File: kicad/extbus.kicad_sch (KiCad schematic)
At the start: 2 parts, among them J1 BUS Slot #1

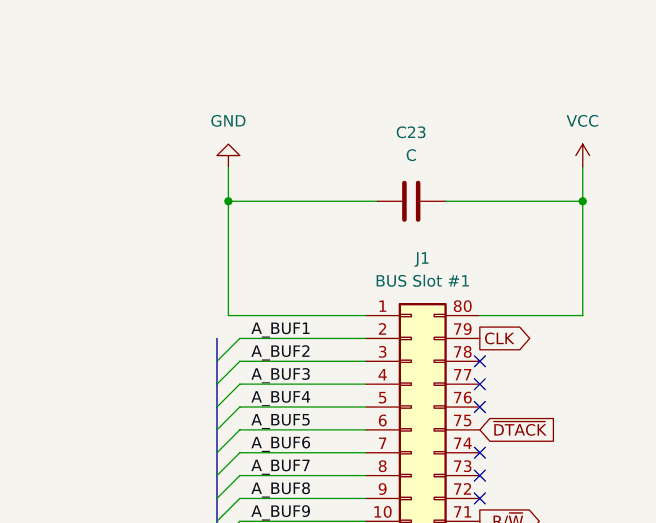
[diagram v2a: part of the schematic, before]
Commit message: added footprints
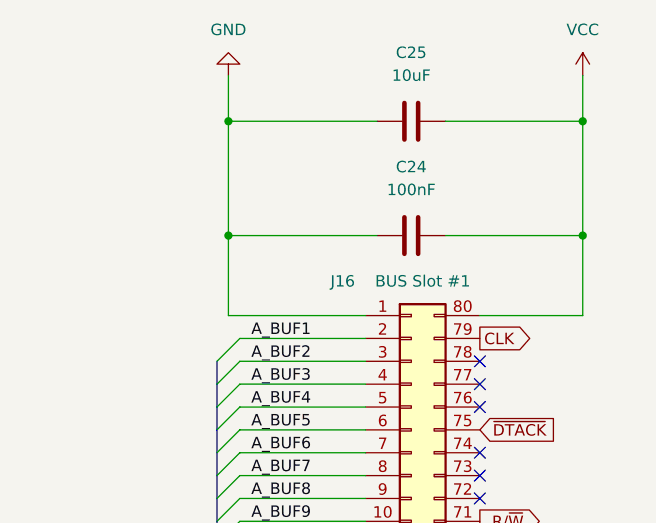
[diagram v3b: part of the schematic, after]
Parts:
- added C25: 10uF, symbol Device:C
- C24: renamed from C23; value C -> 100nF; footprint (none) -> Capacitor_THT:CP_Radial_D5.0mm_P2.50mm
- J16: renamed from J1; footprint (none) -> Connector_PinSocket_2.54mm:PinSocket_2x40_P2.54mm_Vertical
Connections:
- net GND: now also C25.1
- net VCC: now also C25.2
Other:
- moved on the sheet: C24
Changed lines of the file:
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@@
 (kicad_sch (version 20230121) (generator eeschema)
   (paper "A4")
-  (junction (at 54.61 33.02) (diameter 0) (color 0 0 0 0)
-  )
-  (junction (at 93.98 33.02) (diameter 0) (color 0 0 0 0)
+  (junction (at 93.98 24.13) (diameter 0) (color 0 0 0 0)
+  )
+  (junction (at 93.98 36.83) (diameter 0) (color 0 0 0 0)
+  )
+  (junction (at 54.61 36.83) (diameter 0) (color 0 0 0 0)
+  )
+  (junction (at 54.61 24.13) (diameter 0) (color 0 0 0 0)
   )
   (no_connect (at 69.85 137.16))
@@
     (stroke (width 0) (type default))
   )
+  (wire (pts (xy 54.61 24.13) (xy 54.61 36.83))
+    (stroke (width 0) (type default))
+  )
   (bus (pts (xy 93.98 111.76) (xy 93.98 114.3))
     (stroke (width 0) (type default))
   )
-  (wire (pts (xy 54.61 29.21) (xy 54.61 33.02))
-    (stroke (width 0) (type default))
-  )
   (bus (pts (xy 93.98 144.78) (xy 93.98 154.94))
     (stroke (width 0) (type default))
@@
     (stroke (width 0) (type default))
   )
-  (wire (pts (xy 78.74 33.02) (xy 93.98 33.02))
+  (wire (pts (xy 78.74 36.83) (xy 93.98 36.83))
     (stroke (width 0) (type default))
   )
@@
     (stroke (width 0) (type default))
   )
-  (wire (pts (xy 54.61 33.02) (xy 54.61 45.72))
-    (stroke (width 0) (type default))
-  )
   (wire (pts (xy 82.55 104.14) (xy 91.44 104.14))
     (stroke (width 0) (type default))
@@
     (stroke (width 0) (type default))
   )
+  (wire (pts (xy 93.98 24.13) (xy 93.98 36.83))
+    (stroke (width 0) (type default))
+  )
   (bus (pts (xy 53.34 50.8) (xy 53.34 53.34))
     (stroke (width 0) (type default))
@@
     (stroke (width 0) (type default))
   )
-  (wire (pts (xy 93.98 29.21) (xy 93.98 33.02))
-    (stroke (width 0) (type default))
-  )
   (wire (pts (xy 82.55 119.38) (xy 91.44 119.38))
     (stroke (width 0) (type default))
@@
     (stroke (width 0) (type default))
   )
-  (bus (pts (xy 53.34 48.26) (xy 53.34 50.8))
-    (stroke (width 0) (type default))
-  )
   (bus (pts (xy 53.34 104.14) (xy 53.34 106.68))
     (stroke (width 0) (type default))
@@
     (stroke (width 0) (type default))
   )
+  (wire (pts (xy 93.98 36.83) (xy 93.98 45.72))
+    (stroke (width 0) (type default))
+  )
   (bus (pts (xy 53.34 99.06) (xy 53.34 101.6))
     (stroke (width 0) (type default))
@@
     (stroke (width 0) (type default))
   )
+  (wire (pts (xy 54.61 36.83) (xy 54.61 45.72))
+    (stroke (width 0) (type default))
+  )
   (wire (pts (xy 82.55 101.6) (xy 91.44 101.6))
     (stroke (width 0) (type default))
   )
-  (wire (pts (xy 93.98 33.02) (xy 93.98 45.72))
-    (stroke (width 0) (type default))
-  )
   (wire (pts (xy 82.55 106.68) (xy 91.44 106.68))
     (stroke (width 0) (type default))
@@
     (stroke (width 0) (type default))
   )
+  (wire (pts (xy 78.74 24.13) (xy 93.98 24.13))
+    (stroke (width 0) (type default))
+  )
   (wire (pts (xy 55.88 48.26) (xy 69.85 48.26))
     (stroke (width 0) (type default))
@@
     (stroke (width 0) (type default))
   )
+  (wire (pts (xy 93.98 19.05) (xy 93.98 24.13))
+    (stroke (width 0) (type default))
+  )
   (wire (pts (xy 82.55 137.16) (xy 91.44 137.16))
     (stroke (width 0) (type default))
@@
     (stroke (width 0) (type default))
   )
+  (wire (pts (xy 54.61 19.05) (xy 54.61 24.13))
+    (stroke (width 0) (type default))
+  )
   (wire (pts (xy 55.88 66.04) (xy 69.85 66.04))
     (stroke (width 0) (type default))
@@
     (stroke (width 0) (type default))
   )
+  (wire (pts (xy 54.61 24.13) (xy 71.12 24.13))
+    (stroke (width 0) (type default))
+  )
   (wire (pts (xy 55.88 83.82) (xy 69.85 83.82))
     (stroke (width 0) (type default))
@@
     (stroke (width 0) (type default))
   )
-  (wire (pts (xy 71.12 33.02) (xy 54.61 33.02))
+  (wire (pts (xy 71.12 36.83) (xy 54.61 36.83))
     (stroke (width 0) (type default))
   )
@@
     )
   )
-  (symbol (lib_id "power:GND") (at 54.61 29.21 180) (unit 1)
+  (symbol (lib_id "power:GND") (at 54.61 19.05 180) (unit 1)
     (in_bom yes) (on_board yes) (dnp no) (fields_autoplaced)
-    (property "Reference" "#PWR035" (at 54.61 22.86 0)
-      (effects (font (size 1.27 1.27)) hide)
-    )
-    (property "Value" "GND" (at 54.61 24.13 0)
+    (property "Reference" "#PWR063" (at 54.61 12.7 0)
+      (effects (font (size 1.27 1.27)) hide)
+    )
+    (property "Value" "GND" (at 54.61 13.97 0)
       (effects (font (size 1.27 1.27)))
     )
-    (property "Footprint" "" (at 54.61 29.21 0)
-      (effects (font (size 1.27 1.27)) hide)
-    )
-    (property "Datasheet" "" (at 54.61 29.21 0)
+    (property "Footprint" "" (at 54.61 19.05 0)
+      (effects (font (size 1.27 1.27)) hide)
+    )
+    (property "Datasheet" "" (at 54.61 19.05 0)
       (effects (font (size 1.27 1.27)) hide)
     )
@@
       (project "mb68k"
         (path "/e63e39d7-6ac0-4ffd-8aa3-1841a4541b55/6c955f8d-27cd-4aef-8df3-4a7f3323692c"
-          (reference "#PWR035") (unit 1)
+          (reference "#PWR063") (unit 1)
         )
       )
@@
   )
   (symbol (lib_id "Connector_Generic:Conn_02x40_Counter_Clockwise") (at 74.93 93.98 0) (unit 1)
-    (in_bom yes) (on_board yes) (dnp no) (fields_autoplaced)
-    (property "Reference" "J1" (at 76.2 39.37 0)
+    (in_bom yes) (on_board yes) (dnp no)
+    (property "Reference" "J16" (at 67.31 41.91 0)
       (effects (font (size 1.27 1.27)))
     )
@@
       (effects (font (size 1.27 1.27)))
     )
-    (property "Footprint" "" (at 74.93 93.98 0)
+    (property "Footprint" "Connector_PinSocket_2.54mm:PinSocket_2x40_P2.54mm_Vertical" (at 74.93 93.98 0)
       (effects (font (size 1.27 1.27)) hide)
     )
@@
       (project "mb68k"
         (path "/e63e39d7-6ac0-4ffd-8aa3-1841a4541b55/6c955f8d-27cd-4aef-8df3-4a7f3323692c"
-          (reference "J1") (unit 1)
+          (reference "J16") (unit 1)
         )
       )
@@
   (symbol (lib_id "power:VCC") (at 64.77 106.68 90) (unit 1)
     (in_bom yes) (on_board yes) (dnp no) (fields_autoplaced)
-    (property "Reference" "#PWR036" (at 68.58 106.68 0)
+    (property "Reference" "#PWR066" (at 68.58 106.68 0)
       (effects (font (size 1.27 1.27)) hide)
     )
@@
       (project "mb68k"
         (path "/e63e39d7-6ac0-4ffd-8aa3-1841a4541b55/6c955f8d-27cd-4aef-8df3-4a7f3323692c"
-          (reference "#PWR036") (unit 1)
+          (reference "#PWR066") (unit 1)
         )
       )
@@
   (symbol (lib_id "power:GND") (at 91.44 101.6 90) (unit 1)
     (in_bom yes) (on_board yes) (dnp no) (fields_autoplaced)
-    (property "Reference" "#PWR037" (at 97.79 101.6 0)
+    (property "Reference" "#PWR065" (at 97.79 101.6 0)
       (effects (font (size 1.27 1.27)) hide)
     )
@@
       (project "mb68k"
         (path "/e63e39d7-6ac0-4ffd-8aa3-1841a4541b55/6c955f8d-27cd-4aef-8df3-4a7f3323692c"
-          (reference "#PWR037") (unit 1)
+          (reference "#PWR065") (unit 1)
         )
       )
     )
   )
-  (symbol (lib_id "Device:C") (at 74.93 33.02 90) (unit 1)
+  (symbol (lib_id "Device:C") (at 74.93 24.13 90) (unit 1)
     (in_bom yes) (on_board yes) (dnp no) (fields_autoplaced)
-    (property "Reference" "C23" (at 74.93 25.4 90)
+    (property "Reference" "C25" (at 74.93 16.51 90)
       (effects (font (size 1.27 1.27)))
     )
-    (property "Value" "C" (at 74.93 27.94 90)
+    (property "Value" "10uF" (at 74.93 19.05 90)
       (effects (font (size 1.27 1.27)))
     )
-    (property "Footprint" "" (at 78.74 32.0548 0)
-      (effects (font (size 1.27 1.27)) hide)
-    )
-    (property "Datasheet" "~" (at 74.93 33.02 0)
+    (property "Footprint" "" (at 78.74 23.1648 0)
+      (effects (font (size 1.27 1.27)) hide)
+    )
+    (property "Datasheet" "~" (at 74.93 24.13 0)
       (effects (font (size 1.27 1.27)) hide)
     )
@@
       (project "mb68k"
         (path "/e63e39d7-6ac0-4ffd-8aa3-1841a4541b55/6c955f8d-27cd-4aef-8df3-4a7f3323692c"
-          (reference "C23") (unit 1)
+          (reference "C25") (unit 1)
         )
       )
     )
   )
-  (symbol (lib_id "power:VCC") (at 93.98 29.21 0) (unit 1)
+  (symbol (lib_id "Device:C") (at 74.93 36.83 90) (unit 1)
     (in_bom yes) (on_board yes) (dnp no) (fields_autoplaced)
-    (property "Reference" "#PWR034" (at 93.98 33.02 0)
-      (effects (font (size 1.27 1.27)) hide)
-    )
-    (property "Value" "VCC" (at 93.98 24.13 0)
+    (property "Reference" "C24" (at 74.93 29.21 90)
       (effects (font (size 1.27 1.27)))
     )
-    (property "Footprint" "" (at 93.98 29.21 0)
-      (effects (font (size 1.27 1.27)) hide)
-    )
-    (property "Datasheet" "" (at 93.98 29.21 0)
+    (property "Value" "100nF" (at 74.93 31.75 90)
+      (effects (font (size 1.27 1.27)))
+    )
+    (property "Footprint" "Capacitor_THT:CP_Radial_D5.0mm_P2.50mm" (at 78.74 35.8648 0)
+      (effects (font (size 1.27 1.27)) hide)
+    )
+    (property "Datasheet" "~" (at 74.93 36.83 0)
+      (effects (font (size 1.27 1.27)) hide)
+    )
+    (pin "1")
+    (pin "2")
+    (instances
+      (project "mb68k"
+        (path "/e63e39d7-6ac0-4ffd-8aa3-1841a4541b55/6c955f8d-27cd-4aef-8df3-4a7f3323692c"
+          (reference "C24") (unit 1)
+        )
+      )
+    )
+  )
+  (symbol (lib_id "power:VCC") (at 93.98 19.05 0) (unit 1)
+    (in_bom yes) (on_board yes) (dnp no) (fields_autoplaced)
+    (property "Reference" "#PWR064" (at 93.98 22.86 0)
+      (effects (font (size 1.27 1.27)) hide)
+    )
+    (property "Value" "VCC" (at 93.98 13.97 0)
+      (effects (font (size 1.27 1.27)))
+    )
+    (property "Footprint" "" (at 93.98 19.05 0)
+      (effects (font (size 1.27 1.27)) hide)
+    )
+    (property "Datasheet" "" (at 93.98 19.05 0)
       (effects (font (size 1.27 1.27)) hide)
     )
@@
       (project "mb68k"
         (path "/e63e39d7-6ac0-4ffd-8aa3-1841a4541b55/6c955f8d-27cd-4aef-8df3-4a7f3323692c"
-          (reference "#PWR034") (unit 1)
+          (reference "#PWR064") (unit 1)
         )
       )

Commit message: updated readme
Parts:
- added J20, J22: Spare resistors, Connector_PinSocket_2.54mm:PinSocket_1x10_P2.54mm_Vertical, symbol Connector:Conn_01x10_Pin
- added J21: Power bar, Connector_PinSocket_2.54mm:PinSocket_2x11_P2.54mm_Vertical, symbol Connector_Generic:Conn_02x11_Odd_Even
- added R? (x10): 4k7, Resistor_THT:R_Axial_DIN0207_L6.3mm_D2.5mm_P10.16mm_Horizontal, symbol Device:R
- C25: footprint (none) -> Capacitor_THT:CP_Radial_D5.0mm_P2.50mm
- renumbered C24 to C26, J16 to J23
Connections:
- net GND: now also C25.2, C26.2, J23.80 (Pin_80), J21.1 (Pin_1), J21.11 (Pin_11), J21.13 (Pin_13), J21.15 (Pin_15), J21.17 (Pin_17), J21.19 (Pin_19), J21.21 (Pin_21), J21.3 (Pin_3), J21.5 (Pin_5), J21.7 (Pin_7), J21.9 (Pin_9); no longer C25.1, C26.1, J23.1 (Pin_1)
- net VCC: now also C25.1, C26.1, J23.1 (Pin_1), J21.10 (Pin_10), J21.12 (Pin_12), J21.14 (Pin_14), J21.16 (Pin_16), J21.18 (Pin_18), J21.2 (Pin_2), J21.20 (Pin_20), J21.22 (Pin_22), J21.4 (Pin_4), J21.6 (Pin_6), J21.8 (Pin_8); no longer C25.2, C26.2, J23.80 (Pin_80)
- new net: J20.1 (Pin_1), R?.2
- new net: J20.10 (Pin_10), R?.2
- new net: J20.2 (Pin_2), R?.2
- new net: J20.3 (Pin_3), R?.2
- new net: J20.4 (Pin_4), R?.2
- new net: J20.5 (Pin_5), R?.2
- new net: J20.6 (Pin_6), R?.2
- new net: J20.7 (Pin_7), R?.2
- new net: J20.8 (Pin_8), R?.2
- new net: J20.9 (Pin_9), R?.2
- new net: J22.1 (Pin_1), R?.1
- new net: J22.10 (Pin_10), R?.1
- new net: J22.2 (Pin_2), R?.1
- new net: J22.3 (Pin_3), R?.1
- new net: J22.4 (Pin_4), R?.1
- new net: J22.5 (Pin_5), R?.1
- new net: J22.6 (Pin_6), R?.1
- new net: J22.7 (Pin_7), R?.1
- new net: J22.8 (Pin_8), R?.1
- new net: J22.9 (Pin_9), R?.1
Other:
- note added: "Extra pullup / pulldowns for debug/experiment"
- title: (none) -> Mats Brorson 68010 SBC External Bus
- moved on the sheet: C25, C26, J23

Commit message: PCB to ATX size
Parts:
- removed J23: BUS Slot #1, Connector_PinSocket_2.54mm:PinSocket_2x40_P2.54mm_Vertical, symbol Connector_Generic:Conn_02x40_Counter_Clockwise
- added C14: 10uF, Capacitor_THT:CP_Radial_D5.0mm_P2.50mm, symbol Device:C
- added C15: 100nF, Capacitor_THT:CP_Radial_D5.0mm_P2.50mm, symbol Device:C
- added J23: BUS Slot 2, Connector_PinSocket_2.54mm:PinSocket_2x40_P2.54mm_Vertical, symbol Connector_Generic:Conn_02x40_Odd_Even
- added J24: BUS Slot 1, Connector_PinSocket_2.54mm:PinSocket_2x40_P2.54mm_Vertical, symbol Connector_Generic:Conn_02x40_Odd_Even
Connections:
- net CLK: now also J23.4 (Pin_4), J24.4 (Pin_4)
- net GND: now also J21.10 (Pin_10), J21.12 (Pin_12), J21.14 (Pin_14), J21.16 (Pin_16), J21.18 (Pin_18), J21.2 (Pin_2), J21.20 (Pin_20), J21.22 (Pin_22), J21.4 (Pin_4), J21.6 (Pin_6), J21.8 (Pin_8), C14.2, C15.2, J23.2 (Pin_2), J23.46 (Pin_46), J24.2 (Pin_2), J24.46 (Pin_46); no longer J21.1 (Pin_1), J21.11 (Pin_11), J21.13 (Pin_13), J21.15 (Pin_15), J21.17 (Pin_17), J21.19 (Pin_19), J21.21 (Pin_21), J21.3 (Pin_3), J21.5 (Pin_5), J21.7 (Pin_7), J21.9 (Pin_9)
- net VCC: now also J21.1 (Pin_1), J21.11 (Pin_11), J21.13 (Pin_13), J21.15 (Pin_15), J21.17 (Pin_17), J21.19 (Pin_19), J21.21 (Pin_21), J21.3 (Pin_3), J21.5 (Pin_5), J21.7 (Pin_7), J21.9 (Pin_9), C14.1, C15.1, J23.1 (Pin_1), J23.49 (Pin_49), J24.1 (Pin_1), J24.49 (Pin_49); no longer J21.10 (Pin_10), J21.12 (Pin_12), J21.14 (Pin_14), J21.16 (Pin_16), J21.18 (Pin_18), J21.2 (Pin_2), J21.20 (Pin_20), J21.22 (Pin_22), J21.4 (Pin_4), J21.6 (Pin_6), J21.8 (Pin_8)
- net _R/~{W}: now also J23.20 (Pin_20), J24.20 (Pin_20)
- net ~{DTACK}: now also J23.12 (Pin_12), J24.12 (Pin_12)
- net ~{IACK1}: now also J23.51 (Pin_51), J24.51 (Pin_51)
- net ~{IACK2}: now also J23.53 (Pin_53), J24.53 (Pin_53)
- net ~{IACK3}: now also J23.55 (Pin_55), J24.55 (Pin_55)
- net ~{IACK4}: now also J23.57 (Pin_57), J24.57 (Pin_57)
- net ~{IACK5}: now also J23.59 (Pin_59), J24.59 (Pin_59)
- net ~{IACK6}: now also J23.61 (Pin_61), J24.61 (Pin_61)
- net ~{IACK7}: now also J23.63 (Pin_63), J24.63 (Pin_63)
- net ~{IRQ1}: now also J23.32 (Pin_32), J24.32 (Pin_32)
- net ~{IRQ2}: now also J23.34 (Pin_34), J24.34 (Pin_34)
- net ~{IRQ3}: now also J23.36 (Pin_36), J24.36 (Pin_36)
- net ~{IRQ4}: now also J23.38 (Pin_38), J24.38 (Pin_38)
- net ~{IRQ5}: now also J23.40 (Pin_40), J24.40 (Pin_40)
- net ~{IRQ6}: now also J23.42 (Pin_42), J24.42 (Pin_42)
- net ~{IRQ7}: now also J23.44 (Pin_44), J24.44 (Pin_44)
- net ~{_AS}: now also J23.26 (Pin_26), J24.26 (Pin_26)
- net ~{_LDS}: now also J23.22 (Pin_22), J24.22 (Pin_22)
- net ~{_UDS}: now also J23.24 (Pin_24), J24.24 (Pin_24)
- new net A1: J23.47 (Pin_47), J24.47 (Pin_47)
- new net A10: J23.29 (Pin_29), J24.29 (Pin_29)
- new net A11: J23.27 (Pin_27), J24.27 (Pin_27)
- new net A12: J23.25 (Pin_25), J24.25 (Pin_25)
- new net A13: J23.23 (Pin_23), J24.23 (Pin_23)
- new net A14: J23.21 (Pin_21), J24.21 (Pin_21)
- new net A15: J23.19 (Pin_19), J24.19 (Pin_19)
- new net A16: J23.17 (Pin_17), J24.17 (Pin_17)
- new net A17: J23.15 (Pin_15), J24.15 (Pin_15)
- new net A18: J23.13 (Pin_13), J24.13 (Pin_13)
- new net A19: J23.11 (Pin_11), J24.11 (Pin_11)
- new net A2: J23.45 (Pin_45), J24.45 (Pin_45)
- new net A20: J23.9 (Pin_9), J24.9 (Pin_9)
- new net A21: J23.7 (Pin_7), J24.7 (Pin_7)
- new net A22: J23.5 (Pin_5), J24.5 (Pin_5)
- new net A23: J23.3 (Pin_3), J24.3 (Pin_3)
- new net A3: J23.43 (Pin_43), J24.43 (Pin_43)
- new net A4: J23.41 (Pin_41), J24.41 (Pin_41)
- new net A5: J23.39 (Pin_39), J24.39 (Pin_39)
- new net A6: J23.37 (Pin_37), J24.37 (Pin_37)
- new net A7: J23.35 (Pin_35), J24.35 (Pin_35)
- new net A8: J23.33 (Pin_33), J24.33 (Pin_33)
- new net A9: J23.31 (Pin_31), J24.31 (Pin_31)
- new net D0: J23.78 (Pin_78), J24.78 (Pin_78)
- new net D1: J23.76 (Pin_76), J24.76 (Pin_76)
- new net D10: J23.58 (Pin_58), J24.58 (Pin_58)
- new net D11: J23.56 (Pin_56), J24.56 (Pin_56)
- new net D12: J23.54 (Pin_54), J24.54 (Pin_54)
- new net D13: J23.52 (Pin_52), J24.52 (Pin_52)
- new net D14: J23.50 (Pin_50), J24.50 (Pin_50)
- new net D15: J23.48 (Pin_48), J24.48 (Pin_48)
- new net D2: J23.74 (Pin_74), J24.74 (Pin_74)
- new net D3: J23.72 (Pin_72), J24.72 (Pin_72)
- new net D4: J23.70 (Pin_70), J24.70 (Pin_70)
- new net D5: J23.68 (Pin_68), J24.68 (Pin_68)
- new net D6: J23.66 (Pin_66), J24.66 (Pin_66)
- new net D7: J23.64 (Pin_64), J24.64 (Pin_64)
- new net D8: J23.62 (Pin_62), J24.62 (Pin_62)
- new net D9: J23.60 (Pin_60), J24.60 (Pin_60)
- no-connect marks 17 -> 34

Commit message: saving state
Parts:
- removed J21: Power bar, Connector_PinSocket_2.54mm:PinSocket_2x11_P2.54mm_Vertical, symbol Connector_Generic:Conn_02x11_Odd_Even
- added J21: Power bar, Connector_PinSocket_2.54mm:PinSocket_2x10_P2.54mm_Vertical, symbol Connector_Generic:Conn_02x10_Odd_Even
- C25: footprint Capacitor_THT:CP_Radial_D5.0mm_P2.50mm -> Capacitor_THT:C_Disc_D5.0mm_W2.5mm_P2.50mm
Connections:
- net D0: now also J23.40 (Pin_40), J24.40 (Pin_40); no longer J23.78 (Pin_78), J24.78 (Pin_78)
- net D1: now also J23.38 (Pin_38), J24.38 (Pin_38); no longer J23.76 (Pin_76), J24.76 (Pin_76)
- net D10: now also J23.68 (Pin_68), J24.68 (Pin_68); no longer J23.58 (Pin_58), J24.58 (Pin_58)
- net D11: now also J23.70 (Pin_70), J24.70 (Pin_70); no longer J23.56 (Pin_56), J24.56 (Pin_56)
- net D12: now also J23.72 (Pin_72), J24.72 (Pin_72); no longer J23.54 (Pin_54), J24.54 (Pin_54)
- net D13: now also J23.74 (Pin_74), J24.74 (Pin_74); no longer J23.52 (Pin_52), J24.52 (Pin_52)
- net D14: now also J23.76 (Pin_76), J24.76 (Pin_76); no longer J23.50 (Pin_50), J24.50 (Pin_50)
- net D15: now also J23.78 (Pin_78), J24.78 (Pin_78); no longer J23.48 (Pin_48), J24.48 (Pin_48)
- net D2: now also J23.36 (Pin_36), J24.36 (Pin_36); no longer J23.74 (Pin_74), J24.74 (Pin_74)
- net D3: now also J23.34 (Pin_34), J24.34 (Pin_34); no longer J23.72 (Pin_72), J24.72 (Pin_72)
- net D4: now also J23.32 (Pin_32), J24.32 (Pin_32); no longer J23.70 (Pin_70), J24.70 (Pin_70)
- net D5: now also J23.58 (Pin_58), J24.58 (Pin_58); no longer J23.68 (Pin_68), J24.68 (Pin_68)
- net D6: now also J23.60 (Pin_60), J24.60 (Pin_60); no longer J23.66 (Pin_66), J24.66 (Pin_66)
- net D7: now also J23.62 (Pin_62), J24.62 (Pin_62); no longer J23.64 (Pin_64), J24.64 (Pin_64)
- net D8: now also J23.64 (Pin_64), J24.64 (Pin_64); no longer J23.62 (Pin_62), J24.62 (Pin_62)
- net D9: now also J23.66 (Pin_66), J24.66 (Pin_66); no longer J23.60 (Pin_60), J24.60 (Pin_60)
- net GND: now also J23.42 (Pin_42), J24.42 (Pin_42), J21.10 (Pin_10), J21.12 (Pin_12), J21.14 (Pin_14), J21.16 (Pin_16), J21.18 (Pin_18), J21.2 (Pin_2), J21.20 (Pin_20), J21.4 (Pin_4), J21.6 (Pin_6), J21.8 (Pin_8); no longer J23.46 (Pin_46), J24.46 (Pin_46)
- net VCC: now also J21.1 (Pin_1), J21.11 (Pin_11), J21.13 (Pin_13), J21.15 (Pin_15), J21.17 (Pin_17), J21.19 (Pin_19), J21.3 (Pin_3), J21.5 (Pin_5), J21.7 (Pin_7), J21.9 (Pin_9)
- net ~{IACK1}: now also J23.63 (Pin_63), J24.63 (Pin_63); no longer J23.51 (Pin_51), J24.51 (Pin_51)
- net ~{IACK2}: now also J23.61 (Pin_61), J24.61 (Pin_61); no longer J23.53 (Pin_53), J24.53 (Pin_53)
- net ~{IACK3}: now also J23.59 (Pin_59), J24.59 (Pin_59); no longer J23.55 (Pin_55), J24.55 (Pin_55)
- net ~{IACK5}: now also J23.55 (Pin_55), J24.55 (Pin_55); no longer J23.59 (Pin_59), J24.59 (Pin_59)
- net ~{IACK6}: now also J23.53 (Pin_53), J24.53 (Pin_53); no longer J23.61 (Pin_61), J24.61 (Pin_61)
- net ~{IACK7}: now also J23.51 (Pin_51), J24.51 (Pin_51); no longer J23.63 (Pin_63), J24.63 (Pin_63)
- net ~{IRQ1}: now also J23.56 (Pin_56), J24.56 (Pin_56); no longer J23.32 (Pin_32), J24.32 (Pin_32)
- net ~{IRQ2}: now also J23.54 (Pin_54), J24.54 (Pin_54); no longer J23.34 (Pin_34), J24.34 (Pin_34)
- net ~{IRQ3}: now also J23.52 (Pin_52), J24.52 (Pin_52); no longer J23.36 (Pin_36), J24.36 (Pin_36)
- net ~{IRQ4}: now also J23.50 (Pin_50), J24.50 (Pin_50); no longer J23.38 (Pin_38), J24.38 (Pin_38)
- net ~{IRQ5}: now also J23.48 (Pin_48), J24.48 (Pin_48); no longer J23.40 (Pin_40), J24.40 (Pin_40)
- net ~{IRQ6}: now also J23.46 (Pin_46), J24.46 (Pin_46); no longer J23.42 (Pin_42), J24.42 (Pin_42)
- net ~{EXTSEL}: now reaches J23.18 (Pin_18)
- net ~{EXTSEL}: now also J24.18 (Pin_18)
- no-connect marks 34 -> 32

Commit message: saving kicad
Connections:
- net A1: now also J23.41 (Pin_41), J24.41 (Pin_41); no longer J23.47 (Pin_47), J24.47 (Pin_47)
- net A2: now also J23.43 (Pin_43), J24.43 (Pin_43); no longer J23.45 (Pin_45), J24.45 (Pin_45)
- net A3: now also J23.45 (Pin_45), J24.45 (Pin_45); no longer J23.43 (Pin_43), J24.43 (Pin_43)
- net A4: now also J23.47 (Pin_47), J24.47 (Pin_47); no longer J23.41 (Pin_41), J24.41 (Pin_41)
- net _R/~{W}: now also J23.24 (Pin_24), J24.24 (Pin_24); no longer J23.20 (Pin_20), J24.20 (Pin_20)
- net ~{IACK1}: now also J23.59 (Pin_59), J24.59 (Pin_59); no longer J23.63 (Pin_63), J24.63 (Pin_63)
- net ~{IACK3}: now also J23.63 (Pin_63), J24.63 (Pin_63); no longer J23.59 (Pin_59), J24.59 (Pin_59)
- net ~{IACK4}: now also J23.53 (Pin_53), J24.53 (Pin_53); no longer J23.57 (Pin_57), J24.57 (Pin_57)
- net ~{IACK6}: now also J23.57 (Pin_57), J24.57 (Pin_57); no longer J23.53 (Pin_53), J24.53 (Pin_53)
- net ~{_AS}: now also J23.20 (Pin_20), J24.20 (Pin_20); no longer J23.26 (Pin_26), J24.26 (Pin_26)
- net ~{_UDS}: now also J23.26 (Pin_26), J24.26 (Pin_26); no longer J23.24 (Pin_24), J24.24 (Pin_24)
